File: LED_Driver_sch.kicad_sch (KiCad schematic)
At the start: 26 parts, among them J4 B4PS-VH_LF__SN_, J5 Barrel_Jack_Switch, Q1 NMOS, Q2 NMOS, Q3 NMOS, U2 TLV9001TIDCKR

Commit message: Done ERC + Documentation
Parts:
- removed C29: 680uF, footprints:UCL1E681MNL1GS, symbol Device:C
- added C46: 680uF, footprints:UCL1E681MNL1GS, symbol Device:C_Polarized
- C44: renamed from C30; MPN CL10B105KP8NNNC -> CC0603KRX7R9BB105; Manufacturer Samsung Electro-Mechanics -> Yageo
- C45: renamed from C31; footprint Capacitor_SMD:C_0402_1005Metric -> Capacitor_SMD:C_0603_1608Metric; MPN GRM155R71A104KA01D -> GRM188R71H104KA93D
- D11: renamed from D6; footprint DIOM5436X261N -> footprints:SMBJ15A; MPN (none) -> SMBJ15A; Manufacturer_Part_Number SMBJ15A -> (none)
- F1: MPN (none) -> 2920L600/24SL; Manufacturer (none) -> Littlefuse
- J8: renamed from J4; MPN (none) -> B4PS-VH(LF)(SN); Manufacturer_Part_Number B4PS-VH(LF)(SN) -> (none)
- U6: renamed from U2; MPN (none) -> TLV9001TIDCKR
- renumbered C24 to C47, C25 to C48, C26 to C49, C27 to C50, J5 to J7, R17 to R43, R24 to R44, R29 to R45, R30 to R46, R25 to R47, R31 to R48, R26 to R49, R27 to R50, R28 to R51, R33 to R52, R32 to R53
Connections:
- net +12V: now also C46.1
- net GND: now also C46.2
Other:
- note added: "LED switching freq = 2.5kHz Filter Cutoff freq = 154Hz Opamp Gain = 10x"
- moved on the sheet: C47, C48, C49, C50, D11, Q1, Q2, Q3, R43, R44, R45, R46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

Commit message: Initial Review Changes
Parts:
- added C46: 1uF, Capacitor_SMD:C_0603_1608Metric, symbol Device:C
- added C47: 0.1uF, Capacitor_SMD:C_0603_1608Metric, symbol Device:C
- added C49: 100uF, Capacitor_SMD:CP_Elec_6.3x7.7, symbol Device:C_Polarized
- added Q1: PMOS, Package_SO:SOIC-8_5.3x5.3mm_P1.27mm, symbol Simulation_SPICE:PMOS
- added R43: 100k, Resistor_SMD:R_0603_1608Metric, symbol Device:R_US
- added TP6: 12V, TestPoint:TestPoint_Keystone_5000-5004_Miniature, symbol Connector:TestPoint
- added TP7: GND, TestPoint:TestPoint_Keystone_5000-5004_Miniature, symbol Connector:TestPoint
- J7: value Barrel_Jack_Switch -> 12V IN
- J8: value B4PS-VH_LF__SN_ -> 12V RGB LED
- renumbered C46 to C48, C47 to C50, C48 to C51, C49 to C52, C50 to C53, F1 to F2, Q1 to Q2, Q2 to Q3, Q3 to Q4, R43 to R44, R44 to R45, R45 to R46, R46 to R47, R47 to R48, R48 to R49, R49 to R50, R50 to R51, R51 to R52, R52 to R53, R53 to R54
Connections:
- net +12V: now also C46.1, C47.1, C49.1, Q1.3 (S), TP6.1; no longer F2.2
- net GND: now also C46.2, C47.2, C49.2, R43.2, TP7.1
- new net: F2.2, Q1.1 (D)
- new net: Q1.2 (G), R43.1
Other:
- company: (none) -> _electronic_projects
- title: (none) -> DeskNode-F4
- moved on the sheet: C44, C45, C48, C50, C51, C52, C53, D11, F2, J7, J8, Q2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

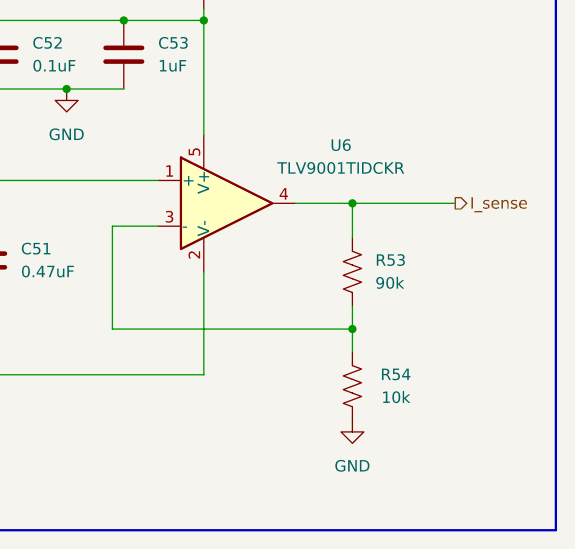
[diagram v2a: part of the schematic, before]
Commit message: MPNs updated
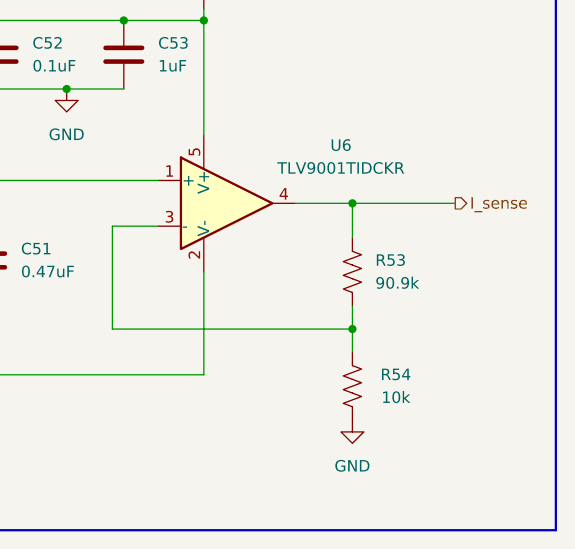
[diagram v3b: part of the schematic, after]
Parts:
- C50, C51: MPN (none) -> CL10B474KA8NFNC
- F2: footprint Fuse:Fuse_2920_7451Metric -> footprints:Fuse_2920_7451Metric; MPN 2920L600/24SL -> 2920L600/24SLER
- Q1: MPN (none) -> FDS6679AZ
- R43, R45, R50, R52: MPN (none) -> RC0603FR-07100KL
- R44, R48, R51: MPN (none) -> RC0603FR-07100RL
- R46: footprint Resistor_SMD:R_1206_3216Metric -> Resistor_SMD:R_2512_6332Metric; MPN (none) -> CRA2512-FZ-R020ELF
- R47, R49: MPN (none) -> RC0603FR-072K2L
- R53: value 90k -> 90.9k; MPN (none) -> RC0603FR-0790K9L
- R54: MPN (none) -> RC0603FR-0710KL

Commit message: Layout placement
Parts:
- removed D11: SMBJ15A, footprints:SMBJ15A, symbol SMBJ15A:SMBJ15A
- added D11: SMBJ15CA, footprints:SMBJ15A, symbol Device:D_TVS
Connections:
- net +12V: now also J8.4; no longer J8.1
- net B_LED: now also J8.3; no longer J8.4
- net GND: now also D11.1 (A1)
- net G_LED: now also J8.2; no longer J8.3
- net R_LED: now also J8.1; no longer J8.2
- net at F2.1, J7.1: now also D11.2 (A2)
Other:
- note added: "B4PS-VH(LF)(SN)"
- moved on the sheet: F2, J8, Q1, R43

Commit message: Layout Routing
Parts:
- added R44: 100k, Resistor_SMD:R_0603_1608Metric, symbol Device:R_US
- added R45: 22.1k, Resistor_SMD:R_0603_1608Metric, symbol Device:R_US
- C49: renamed from C48; MPN UCL1E681MNL1GS -> UCL1E681M
- C50: renamed from C49; MPN UWT1E101MCL1GS -> UWT1E101M
- F2: MPN 2920L600/24SLER -> 2920L600/24
- Q1: MPN FDS6679AZ -> FDS6679
- Q2, Q3, Q4: MPN IRLML6344TRPBF -> IRLML6344
- renumbered C44 to C45, C45 to C47, C47 to C48, C50 to C51, C51 to C52, C52 to C53, C53 to C54, D11 to D12, R44 to R46, R45 to R47, R46 to R48, R47 to R49, R48 to R50, R49 to R51, R50 to R52, R51 to R53, R52 to R54, R53 to R55, R54 to R56
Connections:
- net +12V: now also R44.1
- net GND: now also R45.2
- new net V_sense: R44.2, R45.1
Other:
- note added: "+2.17V"
- moved on the sheet: C45, C46, C47, C48, C49, C50, C51, C52, C53, C54, D12, F2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

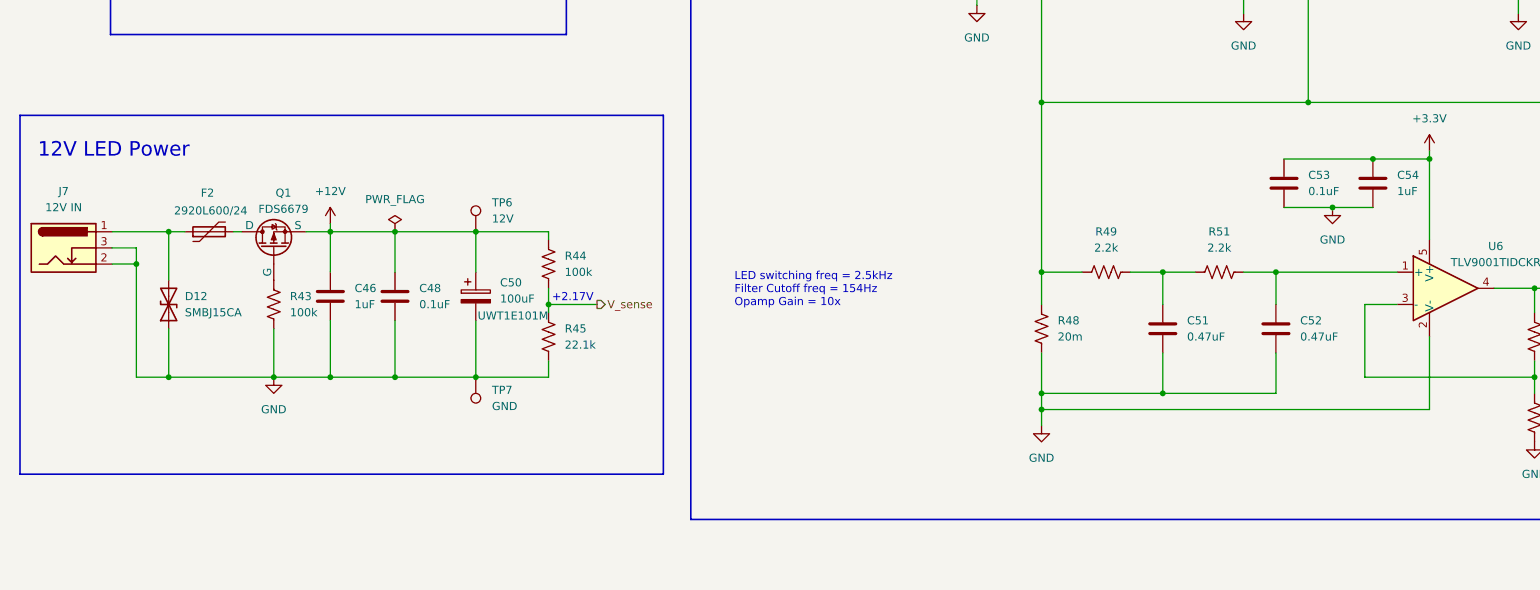
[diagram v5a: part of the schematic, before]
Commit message: Layout - 12V Power path
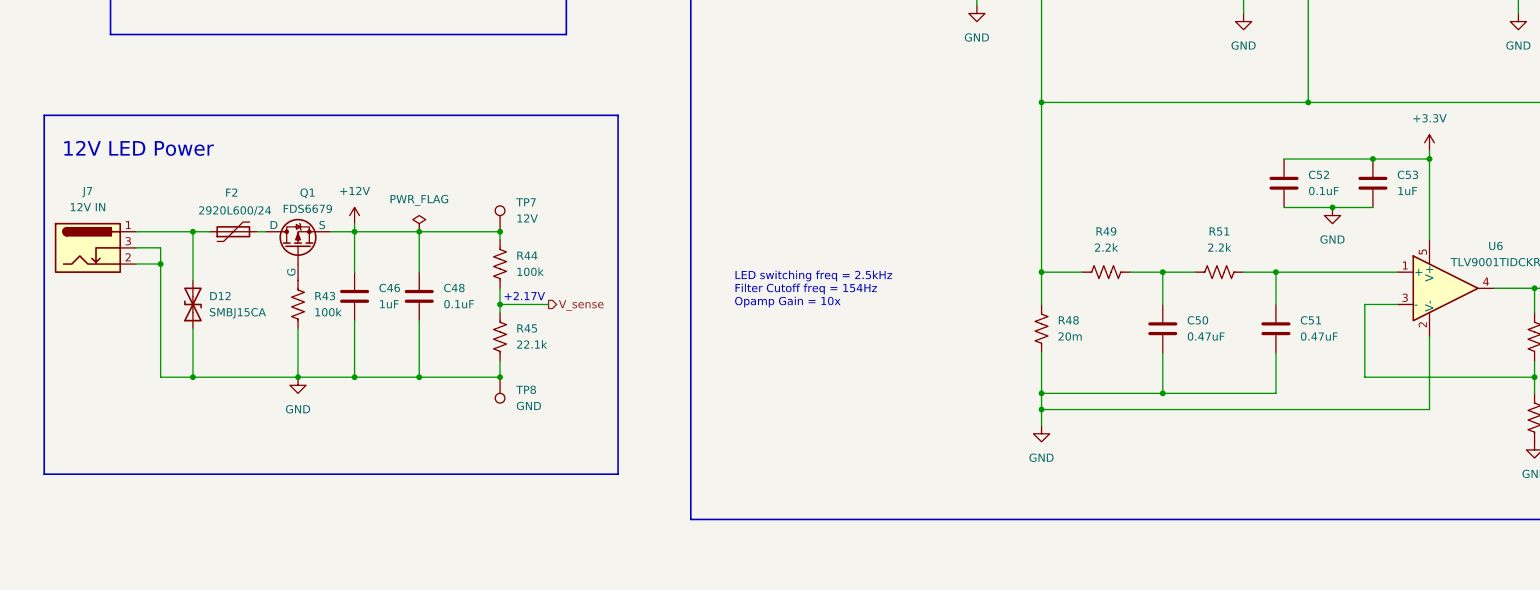
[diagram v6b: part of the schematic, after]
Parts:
- removed C50: 100uF, Capacitor_SMD:CP_Elec_6.3x7.7, symbol Device:C_Polarized
- renumbered C51 to C50, C52 to C51, C53 to C52, C54 to C53, TP6 to TP7, TP7 to TP8
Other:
- moved on the sheet: C46, C48, D12, F2, J7, Q1, R43, R44, R45, TP7, TP8

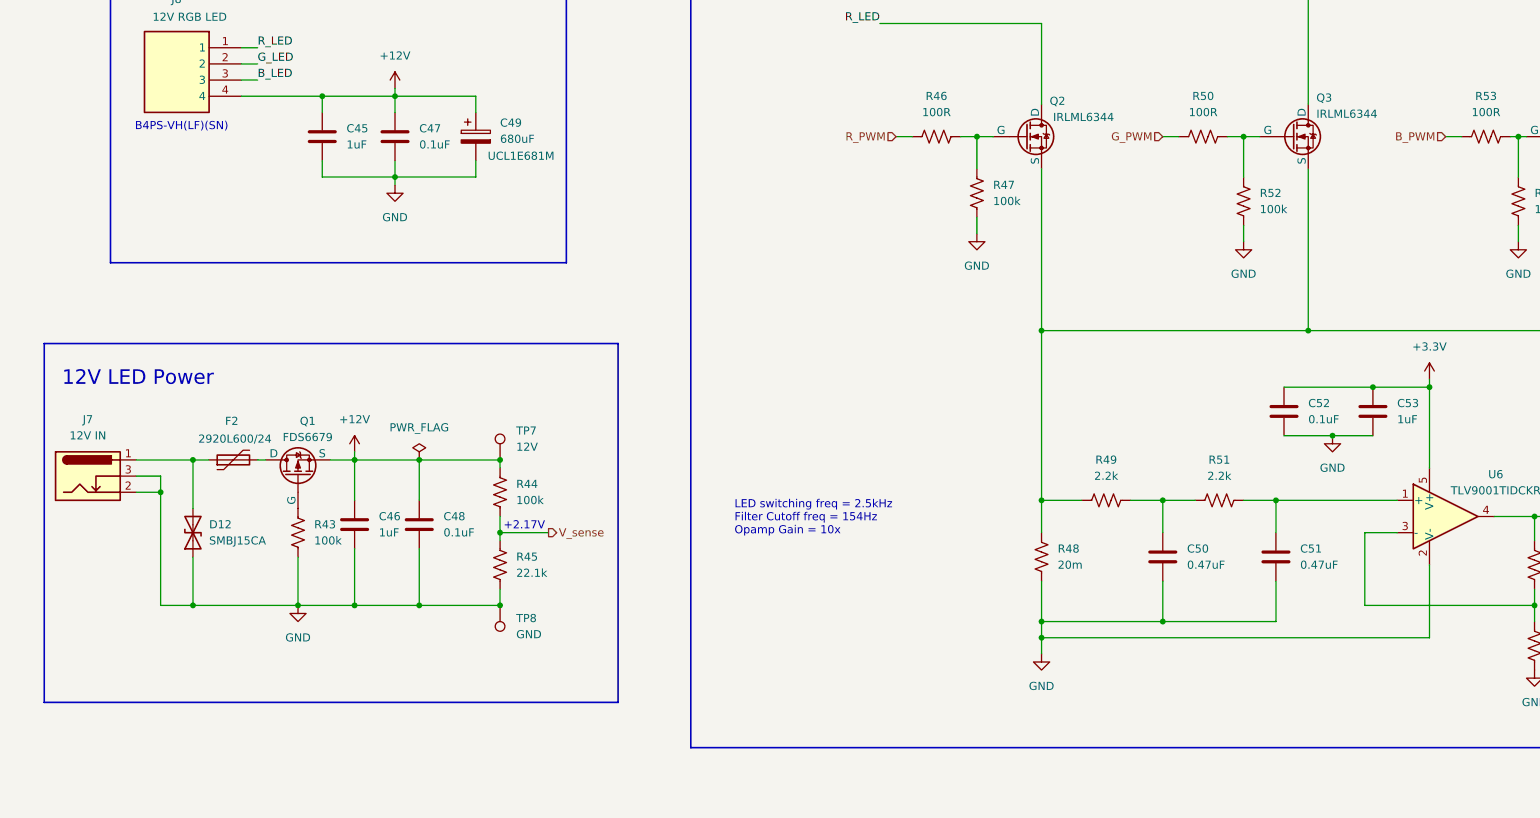
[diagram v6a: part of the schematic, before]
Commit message: 12V i/p FIlter caps removed
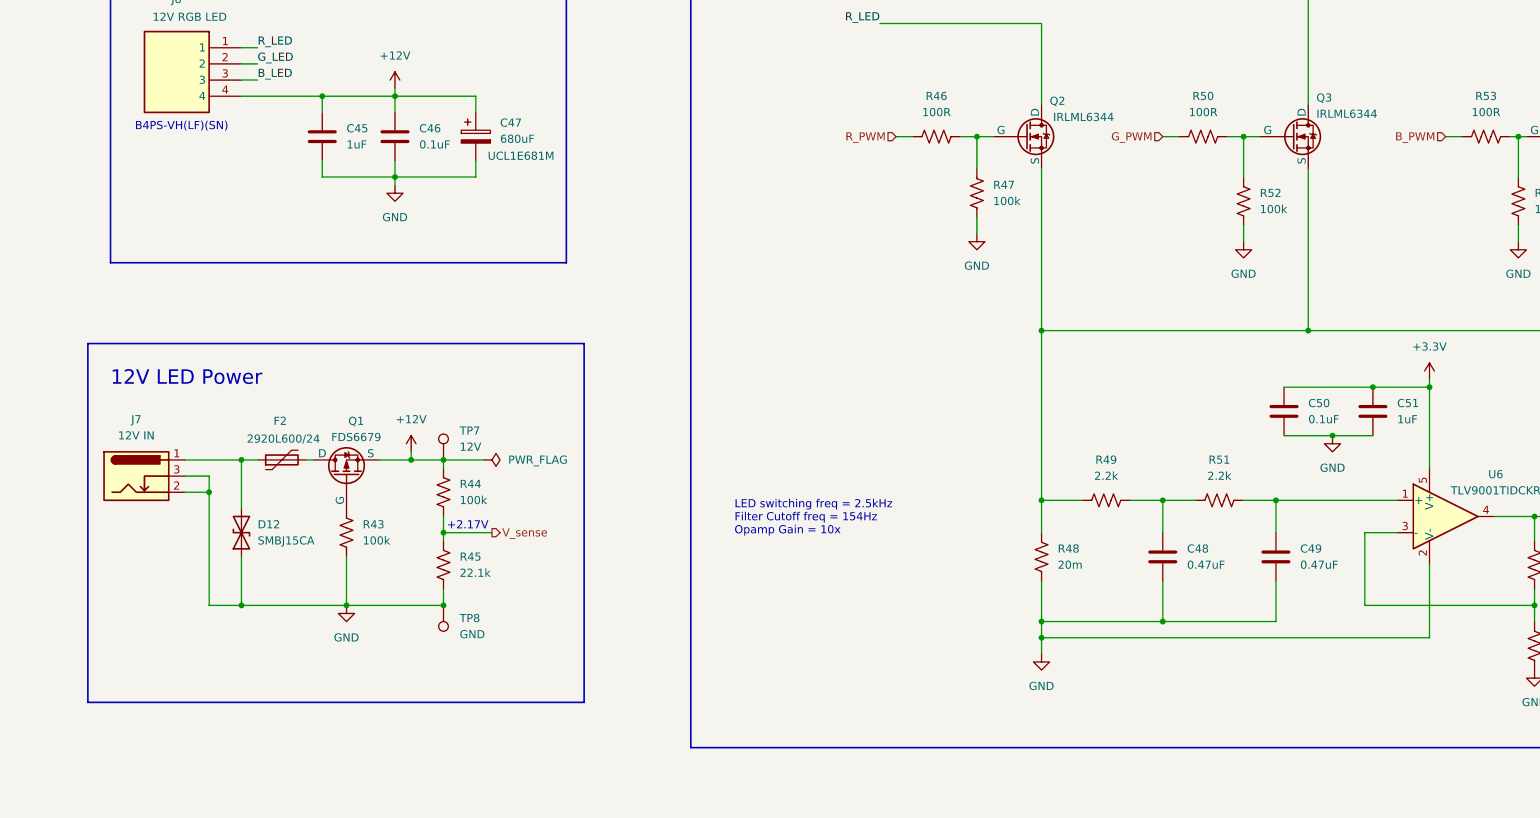
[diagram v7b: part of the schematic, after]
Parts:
- removed C46: 1uF, Capacitor_SMD:C_0603_1608Metric, symbol Device:C
- removed C48: 0.1uF, Capacitor_SMD:C_0603_1608Metric, symbol Device:C
- renumbered C47 to C46, C49 to C47, C50 to C48, C51 to C49, C52 to C50, C53 to C51
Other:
- moved on the sheet: D12, F2, J7, Q1, R43, R44, R45, TP7, TP8

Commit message: Review files
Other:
- company: _electronic_projects -> (none)
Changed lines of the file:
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@@
 		(title "DeskNode-F4")
 		(rev "A")
-		(company "_electronic_projects")
-		(comment 1 "Wajahatulla Sharif")
-		(comment 2 "Designed by ")
 	)
 	(rectangle
